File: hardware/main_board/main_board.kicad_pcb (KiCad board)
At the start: 4 copper layers, 25 x 58 mm, 33 parts, among them J1 eConn_02x03_Odd_Even, P1 CONN_01X02, Q1 DMG3415U, SW1 SW_DPDT_x2, U1 MCP73831/2, U2 AP2112, U3 MCP9808, U4 ESP-WROOM-32D, U5 MMA8451Q

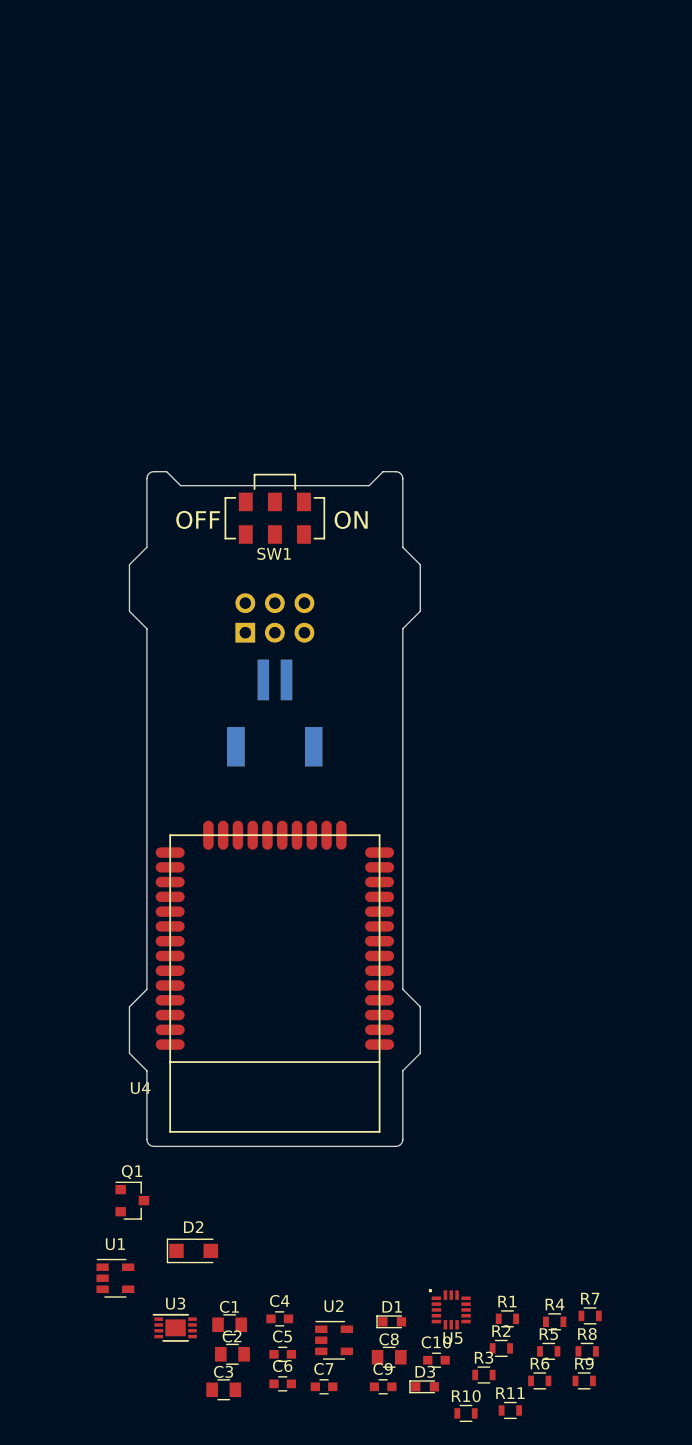
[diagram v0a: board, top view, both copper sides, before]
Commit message: Updated PCB board outline for new tube
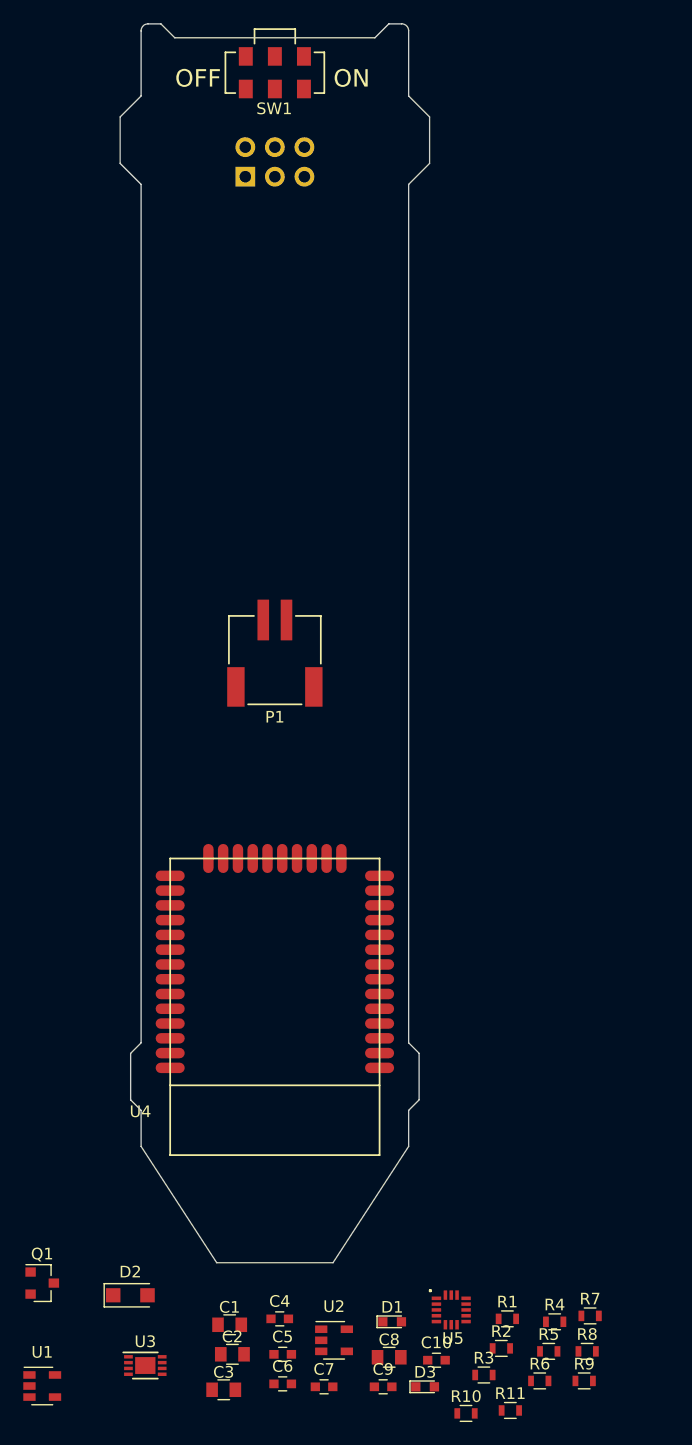
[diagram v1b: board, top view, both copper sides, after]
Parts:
- P1: moved to F.Cu
- moved J1 39.2 mm to (135.5, 33.6)
- moved SW1 38.3 mm to (138.0, 24.7)
- moved U1 11.2 mm to (118.0, 137.6)
- moved Q1 10.5 mm to (118.0, 128.8)
- moved D2 6.64 mm to (125.6, 129.8)
- moved P1 5.15 mm to (138.0, 79.0), turned to 180 degrees
- moved U3 4.15 mm to (126.9, 135.8)
- moved U4 2.00 mm to (138.0, 105.0)
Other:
- board size 25 x 58 mm -> 26.6 x 106.5 mm
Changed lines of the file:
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@@
     (links 81)
     (no_connects 81)
-    (area 125.449999 58.949999 150.550001 117.050001)
+    (area 111.625 19.456646 166.609543 142.4814)
     (thickness 1.2)
     (drawings 31)
@@
   (layers
     (0 F.Cu signal)
-    (1 In1.Cu signal hide)
-    (2 In2.Cu signal hide)
+    (1 In1.Cu signal)
+    (2 In2.Cu signal)
     (31 B.Cu signal)
     (34 B.Paste user)
@@
   )
   (module footprint:SOD-123FL (layer F.Cu)
-    (at 131.015 125.984)
+    (at 125.575 129.8)
     (descr SOD-123)
     (tags SOD-123)
@@
   )
   (module Socket_Strips:Socket_Strip_Angled_2x03_Pitch2.54mm (layer B.Cu)
-    (at 135.46 72.84 270)
+    (at 135.46 33.64 270)
     (descr "Through hole angled socket strip, 2x03, 2.54mm pitch, 8.51mm socket length, double rows")
     (tags "Through hole angled socket strip THT 2x03 2.54mm double row")
@@
     )
   )
-  (module "footprint:S2B-PH-SM4-TB(LF)(SN)" (layer B.Cu)
-    (at 138 84.15)
+  (module "footprint:S2B-PH-SM4-TB(LF)(SN)" (layer F.Cu)
+    (at 138 79 180)
     (descr "JST PH series connector, B2B-PH-SM4-TB, top entry type, surface mount, Datasheet: http://www.jst-mfg.com/product/pdf/eng/ePH.pdf")
     (tags "connector jst ph")
     (attr smd)
-    (fp_text reference P1 (at 0 1.1) (layer B.SilkS)
-      (effects (font (size 1 1) (thickness 0.15)) (justify mirror))
-    )
-    (fp_text value CONN_01X02 (at 0 -4.875) (layer B.Fab) hide
-      (effects (font (size 1 1) (thickness 0.15)) (justify mirror))
-    )
-    (fp_line (start -2.3 0) (end 2.3 0) (layer B.SilkS) (width 0.15))
-    (fp_line (start -3.95 -7.6) (end -3.95 -3.5) (layer B.SilkS) (width 0.15))
-    (fp_line (start 3.95 -7.6) (end 3.95 -3.5) (layer B.SilkS) (width 0.15))
-    (fp_line (start 3.95 -7.6) (end 1.8 -7.6) (layer B.SilkS) (width 0.15))
-    (fp_line (start -3.95 -7.6) (end -1.8 -7.6) (layer B.SilkS) (width 0.15))
-    (pad 2 smd rect (at -1 -7.25) (size 1 3.5) (layers B.Cu B.Paste B.Mask)
-      (net 2 GND))
-    (pad 1 smd rect (at 1 -7.25) (size 1 3.5) (layers B.Cu B.Paste B.Mask)
+    (fp_text reference P1 (at 0 -1.1 180) (layer F.SilkS)
+      (effects (font (size 1 1) (thickness 0.15)))
+    )
+    (fp_text value CONN_01X02 (at 0 4.875 180) (layer F.Fab) hide
+      (effects (font (size 1 1) (thickness 0.15)))
+    )
+    (fp_line (start -2.3 0) (end 2.3 0) (layer F.SilkS) (width 0.15))
+    (fp_line (start -3.95 7.6) (end -3.95 3.5) (layer F.SilkS) (width 0.15))
+    (fp_line (start 3.95 7.6) (end 3.95 3.5) (layer F.SilkS) (width 0.15))
+    (fp_line (start 3.95 7.6) (end 1.8 7.6) (layer F.SilkS) (width 0.15))
+    (fp_line (start -3.95 7.6) (end -1.8 7.6) (layer F.SilkS) (width 0.15))
+    (pad 2 smd rect (at -1 7.25 180) (size 1 3.5) (layers F.Cu F.Paste F.Mask)
+      (net 2 GND))
+    (pad 1 smd rect (at 1 7.25 180) (size 1 3.5) (layers F.Cu F.Paste F.Mask)
       (net 3 +BATT))
-    (pad "" smd rect (at -3.35 -1.5) (size 1.5 3.4) (layers B.Cu B.Paste B.Mask))
-    (pad "" smd rect (at 3.35 -1.5) (size 1.5 3.4) (layers B.Cu B.Paste B.Mask))
+    (pad "" smd rect (at -3.35 1.5 180) (size 1.5 3.4) (layers F.Cu F.Paste F.Mask))
+    (pad "" smd rect (at 3.35 1.5 180) (size 1.5 3.4) (layers F.Cu F.Paste F.Mask))
     (model Connectors_JST.3dshapes/JST_PH_B2B-PH-SM4-TB_02x2.00mm_Straight.wrl
       (at (xyz 0 0 0))
@@
   )
   (module TO_SOT_Packages_SMD:SOT-23 (layer F.Cu)
-    (at 125.746 121.666)
+    (at 118 128.75)
     (descr "SOT-23, Standard")
     (tags SOT-23)
@@
   )
   (module footprint:CL-SB-22A (layer F.Cu)
-    (at 138 63 180)
+    (at 138 24.7 180)
     (fp_text reference SW1 (at 0.05 -3.1 180) (layer F.SilkS)
       (effects (font (size 1 1) (thickness 0.15)))
@@
   )
   (module TO_SOT_Packages_SMD:SOT-23-5 (layer F.Cu)
-    (at 124.29 128.336)
+    (at 118 137.6)
     (descr "5-pin SOT23 package")
     (tags SOT-23-5)
@@
   )
   (module Housings_DFN_QFN:DFN-8-1EP_3x2mm_Pitch0.5mm (layer F.Cu)
-    (at 129.466 132.6)
+    (at 126.8625 135.8375)
     (descr "8-Lead Plastic Dual Flat, No Lead Package (MC) - 2x3x0.9 mm Body [DFN] (see Microchip Packaging Specification 00000049BS.pdf)")
     (tags "DFN 0.5")
@@
   )
   (module footprint:ESP32-WROOM (layer F.Cu)
-    (at 138 103)
+    (at 138 105)
     (fp_text reference U4 (at -11.557 9.017) (layer F.SilkS)
       (effects (font (size 1 1) (thickness 0.15)))
@@
       (net 2 GND))
   )
-  (gr_line (start 149 65.5) (end 149 59.6) (layer Edge.Cuts) (width 0.1))
-  (gr_line (start 129.9 60.2) (end 146.1 60.2) (layer Edge.Cuts) (width 0.1))
-  (gr_line (start 127 65.5) (end 127 59.6) (layer Edge.Cuts) (width 0.1))
-  (gr_line (start 149 103.5) (end 149 72.5) (layer Edge.Cuts) (width 0.1))
-  (gr_line (start 127 103.5) (end 127 72.5) (layer Edge.Cuts) (width 0.1))
-  (gr_line (start 125.5 67) (end 127 65.5) (layer Edge.Cuts) (width 0.1))
-  (gr_line (start 150.5 67) (end 149 65.5) (layer Edge.Cuts) (width 0.1))
-  (gr_line (start 150.5 71) (end 149 72.5) (layer Edge.Cuts) (width 0.1))
-  (gr_line (start 125.5 71) (end 127 72.5) (layer Edge.Cuts) (width 0.1))
-  (gr_line (start 149 110.5) (end 149 116.4) (layer Edge.Cuts) (width 0.1))
-  (gr_line (start 127 116.4) (end 127 110.5) (layer Edge.Cuts) (width 0.1))
-  (gr_line (start 127.6 117) (end 148.4 117) (layer Edge.Cuts) (width 0.1))
-  (gr_line (start 150.5 105) (end 149 103.5) (layer Edge.Cuts) (width 0.1))
-  (gr_line (start 150.5 109) (end 149 110.5) (layer Edge.Cuts) (width 0.1))
-  (gr_line (start 125.5 109) (end 127 110.5) (layer Edge.Cuts) (width 0.1))
-  (gr_line (start 125.5 105) (end 127 103.5) (layer Edge.Cuts) (width 0.1))
-  (gr_text "LiPoly Batt" (at 132.7 80.3 90) (layer B.SilkS)
+  (gr_line (start 133 127) (end 126.5 117) (layer Edge.Cuts) (width 0.1))
+  (gr_line (start 143 127) (end 149.5 117) (layer Edge.Cuts) (width 0.1))
+  (gr_line (start 133 127) (end 143 127) (layer Edge.Cuts) (width 0.1))
+  (gr_line (start 149.5 26.7) (end 149.5 21.1) (layer Edge.Cuts) (width 0.1))
+  (gr_line (start 129.4 21.7) (end 146.6 21.7) (layer Edge.Cuts) (width 0.1))
+  (gr_line (start 126.5 26.7) (end 126.5 21.1) (layer Edge.Cuts) (width 0.1))
+  (gr_line (start 149.5 108.1) (end 149.5 34.3) (layer Edge.Cuts) (width 0.1))
+  (gr_line (start 126.5 108.1) (end 126.5 34.3) (layer Edge.Cuts) (width 0.1))
+  (gr_line (start 124.7 28.5) (end 126.5 26.7) (layer Edge.Cuts) (width 0.1))
+  (gr_line (start 151.3 28.5) (end 149.5 26.7) (layer Edge.Cuts) (width 0.1))
+  (gr_line (start 151.3 32.5) (end 149.5 34.3) (layer Edge.Cuts) (width 0.1))
+  (gr_line (start 124.7 32.5) (end 126.5 34.3) (layer Edge.Cuts) (width 0.1))
+  (gr_line (start 149.5 113.9) (end 149.5 117) (layer Edge.Cuts) (width 0.1))
+  (gr_line (start 126.5 117) (end 126.5 113.9) (layer Edge.Cuts) (width 0.1))
+  (gr_line (start 150.4 109) (end 149.5 108.1) (layer Edge.Cuts) (width 0.1))
+  (gr_line (start 150.4 113) (end 149.5 113.9) (layer Edge.Cuts) (width 0.1))
+  (gr_line (start 125.6 113) (end 126.5 113.9) (layer Edge.Cuts) (width 0.1))
+  (gr_line (start 125.6 109) (end 126.5 108.1) (layer Edge.Cuts) (width 0.1))
+  (gr_text "LiPoly Batt" (at 112.4 77.9 90) (layer B.SilkS)
     (effects (font (size 1 1) (thickness 0.15)) (justify mirror))
   )
-  (gr_text "OFF\n" (at 131.4 63.2) (layer F.SilkS)
+  (gr_text "OFF\n" (at 131.4 25.2) (layer F.SilkS)
     (effects (font (size 1.5 1.5) (thickness 0.3)))
   )
-  (gr_text ON (at 144.6 63.2) (layer F.SilkS)
+  (gr_text ON (at 144.6 25.2) (layer F.SilkS)
     (effects (font (size 1.5 1.5) (thickness 0.3)))
   )
-  (gr_line (start 148.4 59) (end 147.3 59) (layer Edge.Cuts) (width 0.1))
-  (gr_line (start 127.6 59) (end 128.7 59) (layer Edge.Cuts) (width 0.1))
-  (gr_arc (start 127.6 116.4) (end 127.6 117) (angle 90) (layer Edge.Cuts) (width 0.1))
-  (gr_arc (start 148.4 116.4) (end 149 116.4) (angle 90) (layer Edge.Cuts) (width 0.1))
-  (gr_arc (start 148.4 59.6) (end 148.4 59) (angle 90) (layer Edge.Cuts) (width 0.1))
-  (gr_arc (start 127.6 59.6) (end 127 59.6) (angle 90) (layer Edge.Cuts) (width 0.1))
-  (gr_line (start 147.3 59) (end 146.1 60.2) (layer Edge.Cuts) (width 0.1))
-  (gr_line (start 128.7 59) (end 129.9 60.2) (layer Edge.Cuts) (width 0.1))
-  (gr_line (start 150.5 105) (end 150.5 109) (layer Edge.Cuts) (width 0.1))
-  (gr_line (start 150.5 67) (end 150.5 71) (layer Edge.Cuts) (width 0.1))
-  (gr_line (start 125.5 71) (end 125.5 67) (layer Edge.Cuts) (width 0.1))
-  (gr_line (start 125.5 109) (end 125.5 105) (layer Edge.Cuts) (width 0.1))
+  (gr_line (start 148.9 20.5) (end 147.8 20.5) (layer Edge.Cuts) (width 0.1))
+  (gr_line (start 127.1 20.5) (end 128.2 20.5) (layer Edge.Cuts) (width 0.1))
+  (gr_arc (start 148.9 21.1) (end 148.9 20.5) (angle 90) (layer Edge.Cuts) (width 0.1))
+  (gr_arc (start 127.1 21.1) (end 126.5 21.1) (angle 90) (layer Edge.Cuts) (width 0.1))
+  (gr_line (start 147.8 20.5) (end 146.6 21.7) (layer Edge.Cuts) (width 0.1))
+  (gr_line (start 128.2 20.5) (end 129.4 21.7) (layer Edge.Cuts) (width 0.1))
+  (gr_line (start 150.4 109) (end 150.4 113) (layer Edge.Cuts) (width 0.1))
+  (gr_line (start 151.3 28.5) (end 151.3 32.5) (layer Edge.Cuts) (width 0.1))
+  (gr_line (start 124.7 32.5) (end 124.7 28.5) (layer Edge.Cuts) (width 0.1))
+  (gr_line (start 125.6 113) (end 125.6 109) (layer Edge.Cuts) (width 0.1))
   (zone (net 2) (net_name GND) (layer In1.Cu) (hatch edge 0.508)
     (connect_pads (clearance 0.2))
@@
     (polygon
       (pts
-        (xy 127 58) (xy 149 58) (xy 149 109) (xy 127 109)
+        (xy 124 20) (xy 152 20) (xy 152 130) (xy 124 130)
       )
     )
@@
     (polygon
       (pts
-        (xy 127 58) (xy 149 58) (xy 149 109) (xy 127 109)
+        (xy 124 20) (xy 152 20) (xy 152 130) (xy 124 130)
       )
     )

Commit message: Working on component placement
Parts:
- moved C1 106.1 mm to (147.0, 27.0)
- moved C3 105.0 mm to (145.5, 33.6), turned to 180 degrees
- moved U2 103.4 mm to (145.2, 30.3), turned to 270 degrees
- moved D2 102.5 mm to (130.2, 27.4), turned to 180 degrees
- moved R1 101.9 mm to (130.2, 33.8)
- moved C4 101.7 mm to (148.2, 30.6), turned to 90 degrees
- moved Q1 98.7 mm to (130.2, 30.8), turned to 180 degrees
- moved U1 67.3 mm to (142.2, 74.8), turned to 270 degrees
- moved R6 62.1 mm to (142.2, 77.9)
- moved R2 60.9 mm to (145.2, 74.7), turned to 270 degrees
- moved C2 60.3 mm to (139.0, 74.8), turned to 270 degrees
- moved D3 58.7 mm to (147.0, 79.1), turned to 270 degrees
- moved R3 57.9 mm to (144.4, 79.9), turned to 180 degrees
- moved D1 57.4 mm to (147.0, 74.7), turned to 90 degrees
- moved C10 53.6 mm to (137.8, 83.7), turned to 180 degrees
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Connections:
- Q1 pad 2: (no net) -> /VIN
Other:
- board text added: "0"
- board text added: "10"
- board text added: "20"
- board text added: "30"
- board text added: "40"
- board text added: "50"
- board text added: "60"
- board text added: "70"
- board text added: "80"
- board text added: "BATTERY"
- board text removed: "LiPoly Batt"

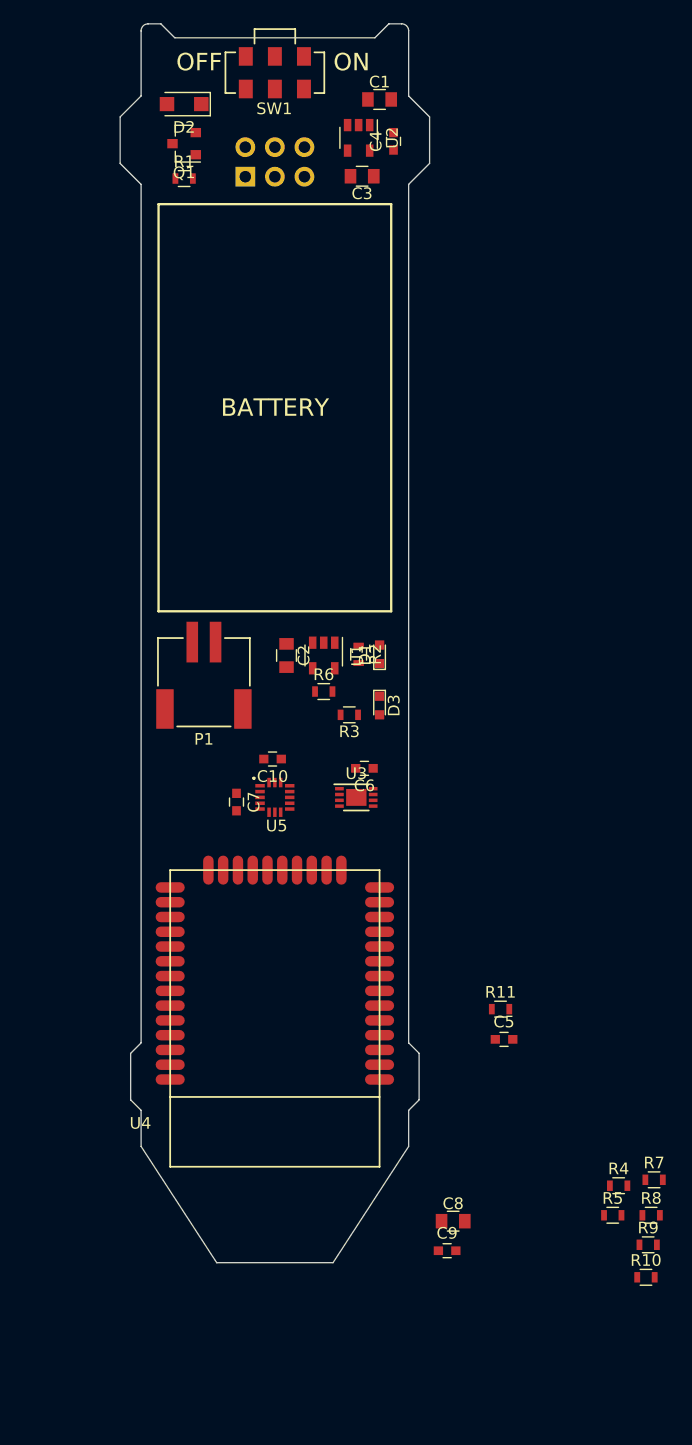
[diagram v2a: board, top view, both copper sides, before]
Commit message: Added UV sensor.  Working on layout
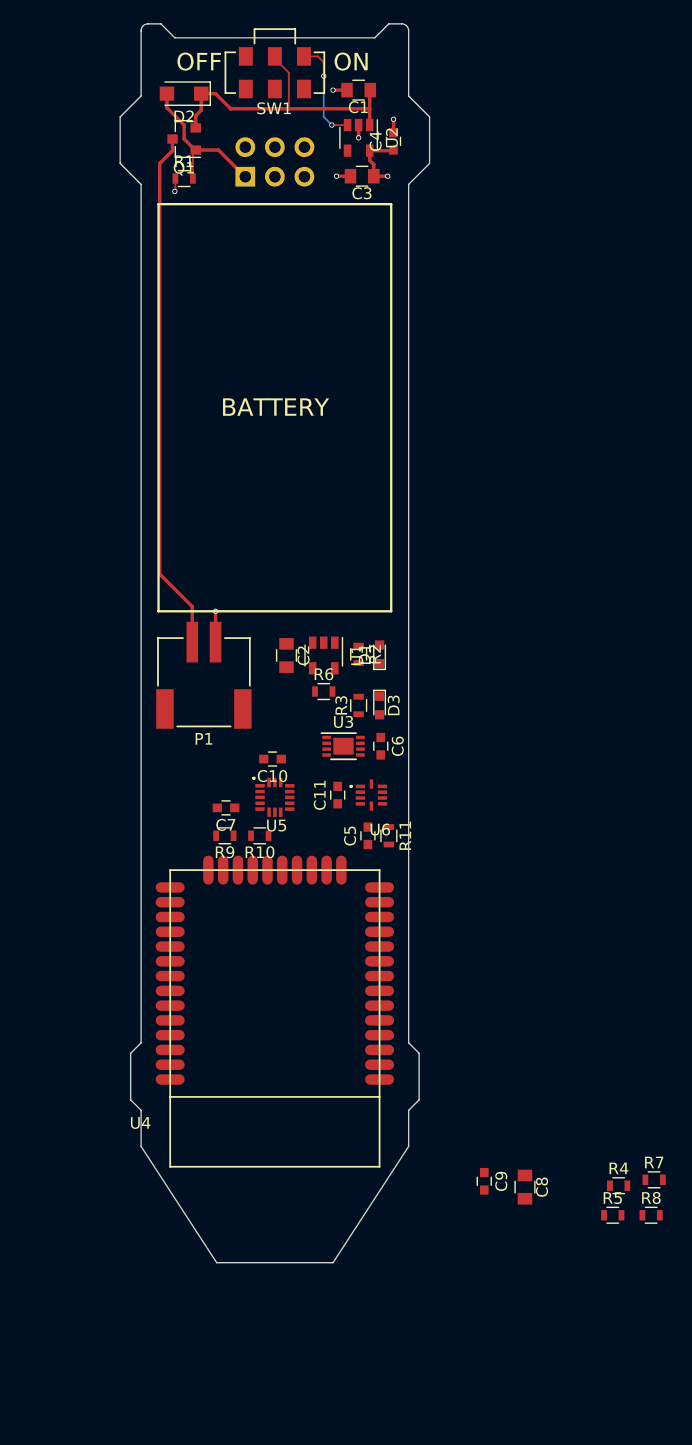
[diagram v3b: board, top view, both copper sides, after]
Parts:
- added C11: 0.1u, Capacitors_SMD:C_0603, F.Cu at (143.4, 86.8)
- added U6: Si1145, footprint:Si1145, F.Cu at (146.3, 86.8)
- moved R9 50.6 mm to (133.7, 90.3), turned to 180 degrees
- moved R10 50.4 mm to (136.7, 90.3), turned to 180 degrees
- moved C5 21.1 mm to (146.0, 90.3), turned to 90 degrees
- moved R11 17.7 mm to (147.8, 90.3), turned to 270 degrees
- moved C8 6.83 mm to (159.5, 120.5), turned to 270 degrees
- moved C9 6.77 mm to (156.0, 120.0), turned to 270 degrees
- moved U3 4.54 mm to (143.9, 82.6)
- moved C6 2.36 mm to (147.1, 82.6), turned to 270 degrees
- moved C1 1.97 mm to (145.2, 26.2), turned to 180 degrees
- moved R3 1.13 mm to (145.2, 79.1), turned to 90 degrees
- moved C7 1.03 mm to (133.8, 87.9), turned to 180 degrees
- moved D2 0.90 mm to (130.2, 26.5)
- moved Q1 0.40 mm to (130.2, 30.4)
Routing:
- net +BATT: track 0.00 -> 44.9 mm
- net /VIN: track 0.00 -> 26.2 mm
- net +5V: track 0.00 -> 13.7 mm
- net Net-(SW1-Pad1): track 0.00 -> 8.95 mm, vias 0 -> 2
- net GND: track 0.00 -> 8.42 mm, vias 0 -> 6
- net +3V3: track 0.00 -> 5.62 mm, vias 0 -> 1

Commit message: Working on layout
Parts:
- removed the C8 at (159.5, 120.5)
- removed the C9 at (156.0, 120.0)
- moved R5 51.6 mm to (138.6, 79.9)
- moved R4 51.4 mm to (138.6, 77.9)
- moved R7 39.7 mm to (146.7, 91.0), turned to 180 degrees
- moved R6 39.0 mm to (146.7, 89.0)
- moved C6 4.34 mm to (141.7, 89.7)
- moved R11 4.04 mm to (143.8, 89.7)
- moved R10 1.60 mm to (138.3, 90.3), turned to 0 degrees
- moved R9 1.20 mm to (134.9, 90.3)
- moved C3 1.10 mm to (143.3, 85.7)
- moved U3 0.90 mm to (146.3, 85.9)
- moved U4 0.78 mm to (143.3, 82.1)
- moved D3 0.58 mm to (147.3, 78.6), turned to 90 degrees
- moved C7 0.54 mm to (147.3, 82.1)
- moved R3 0.51 mm to (145.3, 78.6), turned to 270 degrees
- moved C2 0.40 mm to (138.6, 74.8)
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- renumbered C11 to C3, C3 to C4, C4 to C5, C5 to C6, C6 to C7, C7 to C8, C10 to C9, R7 to R6, R8 to R7, R6 to R8, U6 to U3, U3 to U4, U4 to U5, U5 to U6
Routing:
- net /SDA: track 0.00 -> 54.6 mm, vias 0 -> 6
- net /SCL: track 0.00 -> 48.1 mm, vias 0 -> 4
- net /RESET: track 0.00 -> 24.6 mm
- net /5V_SENSE: track 0.00 -> 19.1 mm
- net GND: track 8.42 -> 24.3 mm, vias 6 -> 19
- net +3V3: track 5.62 -> 19.4 mm, vias 1 -> 10
- net Net-(C8-Pad1): track 0.00 -> 3.24 mm
